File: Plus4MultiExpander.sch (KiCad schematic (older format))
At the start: 11 parts, among them CN1 EDGE_CONN, CN2 C16_NEWSTYLE_EXP_PORT_1, CN3 C16_NEWSTYLE_EXP_PORT_2, CN4 C16_NEWSTYLE_EXP_PORT_3, U1 74LS245, U2 74LS245

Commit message: Add 3D model of connector
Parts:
- CN2, CN3, CN4: MouserPN (none) -> 571-5530843-4
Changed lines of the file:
@@
 F 2 "Plus4MultiExpander:C64-Cart-Socket-Vertical" H 5425 960 50  0001 C CNN
 F 3 "DOCUMENTATION" H 5425 860 50  0001 C CNN
+F 4 "571-5530843-4" H 5425 2410 50  0001 C CNN "MouserPN"
 	1    5425 2410
 	1    0    0    -1
@@
 F 2 "Plus4MultiExpander:C64-Cart-Socket-Vertical" H 5425 4365 50  0001 C CNN
 F 3 "DOCUMENTATION" H 5425 4265 50  0001 C CNN
+F 4 "571-5530843-4" H 5425 5815 50  0001 C CNN "MouserPN"
 	1    5425 5815
 	1    0    0    -1
@@
 F 2 "Plus4MultiExpander:C64-Cart-Socket-Vertical" H 2395 4365 50  0001 C CNN
 F 3 "DOCUMENTATION" H 2395 4265 50  0001 C CNN
+F 4 "571-5530843-4" H 2395 5815 50  0001 C CNN "MouserPN"
 	1    2395 5815
 	1    0    0    -1

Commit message: Add credits and license
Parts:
- added C3: 220u, Capacitor_THT:CP_Radial_D8.0mm_P3.50mm, symbol Device:CP1
- added V0: LICENSE, Plus4MultiExpander:cc_by_nc_sa, symbol void:Void
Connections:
- wire segments 267 -> 269
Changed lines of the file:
@@
 Sheet 1 1
 Title "Plus4MultiExpander"
-Date "2023-07-26"
+Date "2023-08-03"
 Rev "1git"
 Comp "SukkoPera"
 Comment1 "Inspired by Solder/Synergy's Expansionport-Splitter"
-Comment2 ""
+Comment2 "Licensed under CC BY-NC-SA 4.0"
 Comment3 ""
 Comment4 ""
@@
 Text Notes 9710 4580 0    50   ~ 0
 C2 CREATION
+$Comp
+L power:+5V #PWR018
+U 1 1 66854472
+P 10245 2750
+F 0 "#PWR018" H 10245 2600 50  0001 C CNN
+F 1 "+5V" H 10260 2923 50  0000 C CNN
+F 2 "" H 10245 2750 50  0001 C CNN
+F 3 "" H 10245 2750 50  0001 C CNN
+	1    10245 2750
+	1    0    0    -1
+$EndComp
+Wire Wire Line
+	10245 2750 10245 2860
+Wire Wire Line
+	10245 3160 10245 3270
+$Comp
+L power:GND #PWR019
+U 1 1 6685447E
+P 10245 3270
+F 0 "#PWR019" H 10245 3020 50  0001 C CNN
+F 1 "GND" H 10250 3097 50  0000 C CNN
+F 2 "" H 10245 3270 50  0001 C CNN
+F 3 "" H 10245 3270 50  0001 C CNN
+	1    10245 3270
+	-1   0    0    -1
+$EndComp
 Wire Bus Line
 	1045 2645 1045 3345
@@
 Wire Bus Line
 	1045 5865 1045 6565
+$Comp
+L Device:CP1 C3
+U 1 1 66870BF0
+P 10245 3010
+F 0 "C3" H 10360 3056 50  0000 L CNN
+F 1 "220u" H 10360 2965 50  0000 L CNN
+F 2 "Capacitor_THT:CP_Radial_D8.0mm_P3.50mm" H 10245 3010 50  0001 C CNN
+F 3 "~" H 10245 3010 50  0001 C CNN
+	1    10245 3010
+	1    0    0    -1
+$EndComp
+$Comp
+L void:Void V0
+U 1 1 66878EB4
+P 6540 7655
+F 0 "V0" H 6618 7701 50  0000 L CNN
+F 1 "LICENSE" H 6618 7610 50  0000 L CNN
+F 2 "Plus4MultiExpander:cc_by_nc_sa" H 6540 7655 50  0001 C CNN
+F 3 "" H 6540 7655 50  0001 C CNN
+	1    6540 7655
+	1    0    0    -1
+$EndComp
 $EndSCHEMATC

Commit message: Generate /C2 with NAND gate
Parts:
- removed D1, D2: 1n4148, Diode_THT:D_DO-35_SOD27_P7.62mm_Horizontal, symbol Device:D
- removed R1: 4.7k, Resistor_THT:R_Axial_DIN0204_L3.6mm_D1.6mm_P7.62mm_Horizontal, symbol Device:R
- added C4: 100n, Capacitor_THT:C_Disc_D7.0mm_W2.5mm_P5.00mm, symbol Device:C
- added U3: 74HCT00, Package_DIP:DIP-14_W7.62mm_Socket_LongPads, symbol 74xx:74HCT00
- U1, U2: value 74LS245 -> 74HCT245
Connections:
- wire segments 269 -> 287
- no-connect marks 0 -> 2
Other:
- note added: "C2 GENERATION"
- note added: "POWER"
- note added: "SPARES"
- note removed: "C2 CREATION"
- moved on the sheet: C3

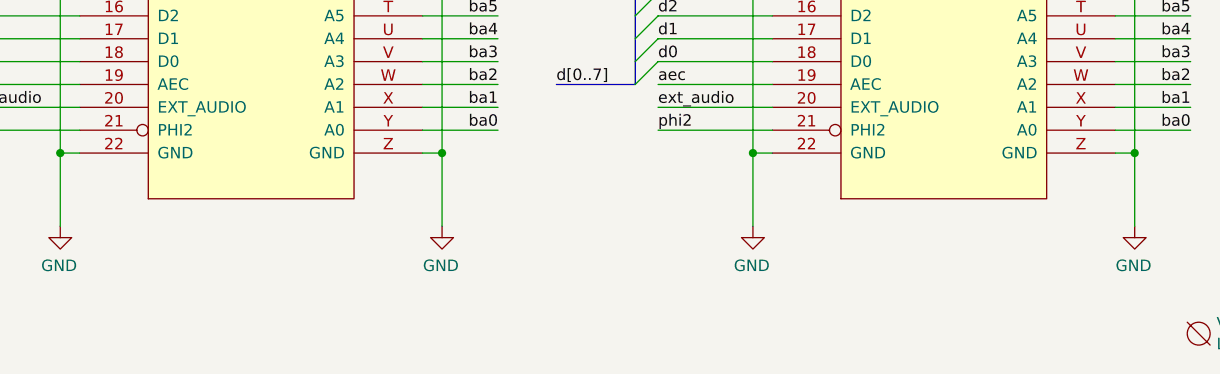
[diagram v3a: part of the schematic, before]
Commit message: Add standoff holes
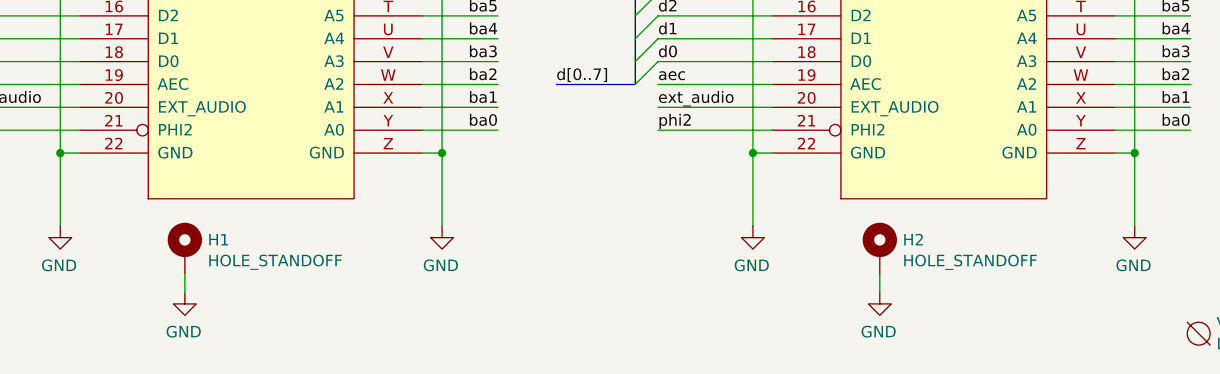
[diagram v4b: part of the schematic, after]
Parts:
- added H1, H2: HOLE_STANDOFF, MountingHole:MountingHole_2.5mm_Pad, symbol Mechanical:MountingHole_Pad
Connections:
- net GND: now also H1.1, H2.1
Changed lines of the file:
@@
 Text Notes 7620 5715 0    50   ~ 0
 SPARES
+$Comp
+L Mechanical:MountingHole_Pad H1
+U 1 1 653ED8E7
+P 2105 7295
+F 0 "H1" H 2205 7344 50  0000 L CNN
+F 1 "HOLE_STANDOFF" H 2205 7253 50  0000 L CNN
+F 2 "MountingHole:MountingHole_2.5mm_Pad" H 2105 7295 50  0001 C CNN
+F 3 "~" H 2105 7295 50  0001 C CNN
+	1    2105 7295
+	1    0    0    -1
+$EndComp
+$Comp
+L power:GND #PWR023
+U 1 1 653EEC4A
+P 2105 7475
+F 0 "#PWR023" H 2105 7225 50  0001 C CNN
+F 1 "GND" H 2110 7302 50  0000 C CNN
+F 2 "" H 2105 7475 50  0001 C CNN
+F 3 "" H 2105 7475 50  0001 C CNN
+	1    2105 7475
+	-1   0    0    -1
+$EndComp
+Wire Wire Line
+	2105 7475 2105 7395
+$Comp
+L Mechanical:MountingHole_Pad H2
+U 1 1 6542A464
+P 5145 7295
+F 0 "H2" H 5245 7344 50  0000 L CNN
+F 1 "HOLE_STANDOFF" H 5245 7253 50  0000 L CNN
+F 2 "MountingHole:MountingHole_2.5mm_Pad" H 5145 7295 50  0001 C CNN
+F 3 "~" H 5145 7295 50  0001 C CNN
+	1    5145 7295
+	1    0    0    -1
+$EndComp
+$Comp
+L power:GND #PWR024
+U 1 1 6542AB06
+P 5145 7475
+F 0 "#PWR024" H 5145 7225 50  0001 C CNN
+F 1 "GND" H 5150 7302 50  0000 C CNN
+F 2 "" H 5145 7475 50  0001 C CNN
+F 3 "" H 5145 7475 50  0001 C CNN
+	1    5145 7475
+	-1   0    0    -1
+$EndComp
+Wire Wire Line
+	5145 7475 5145 7395
 Wire Bus Line
 	1045 2645 1045 3345

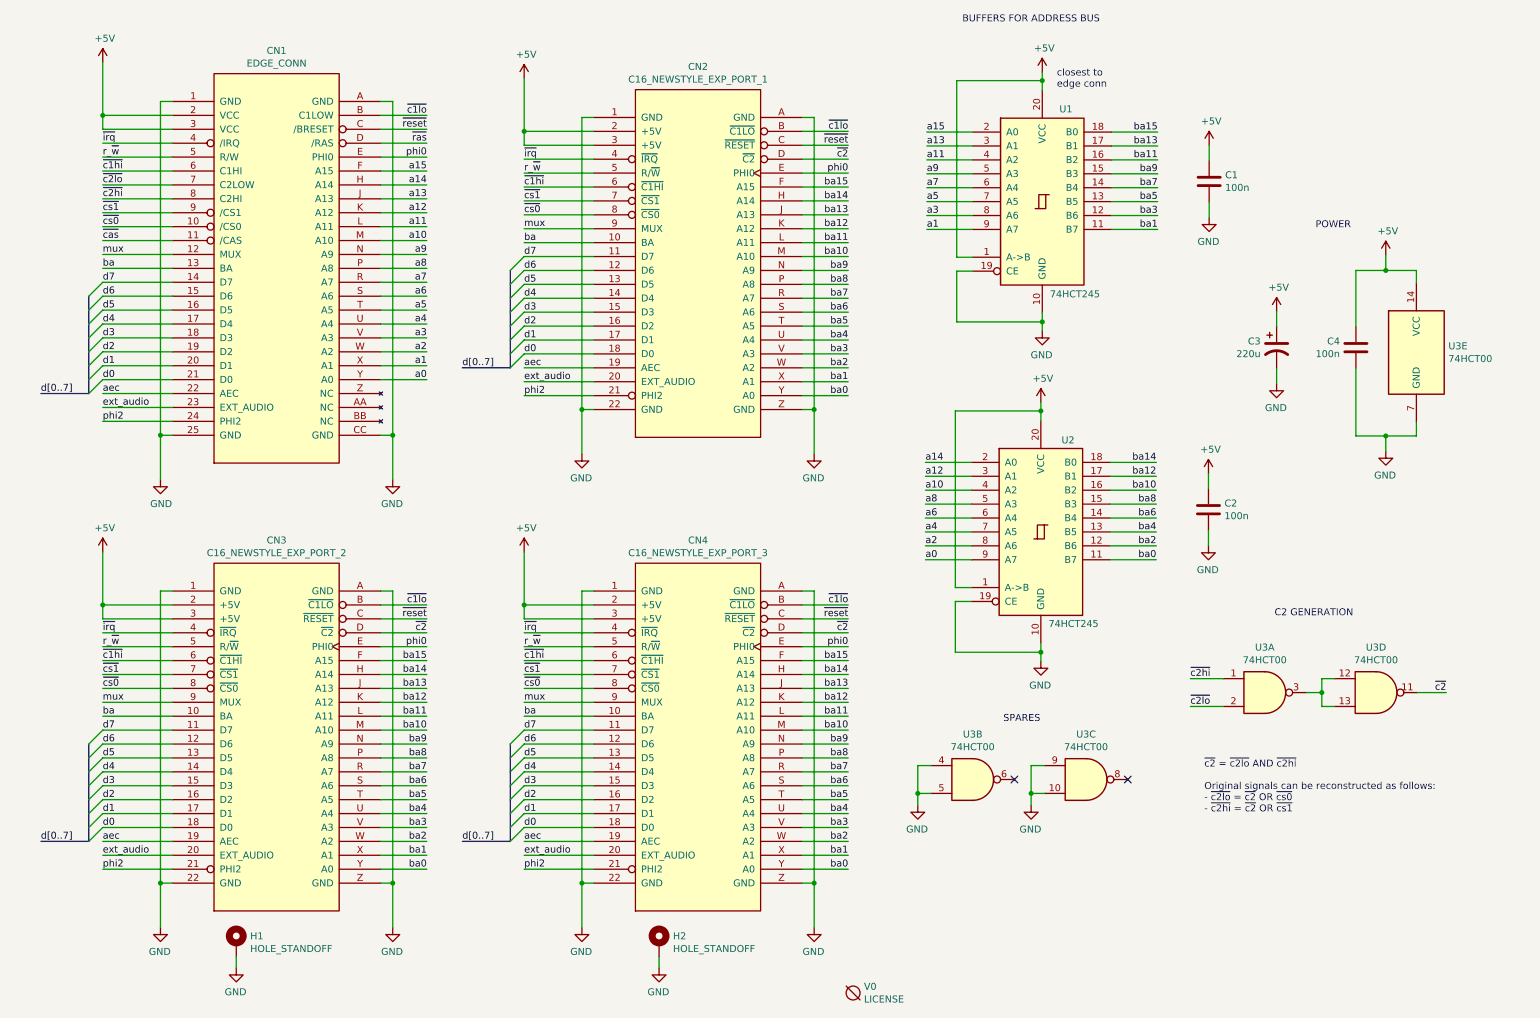
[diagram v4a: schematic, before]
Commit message: Add mixing resistors for EXT_AUDIO
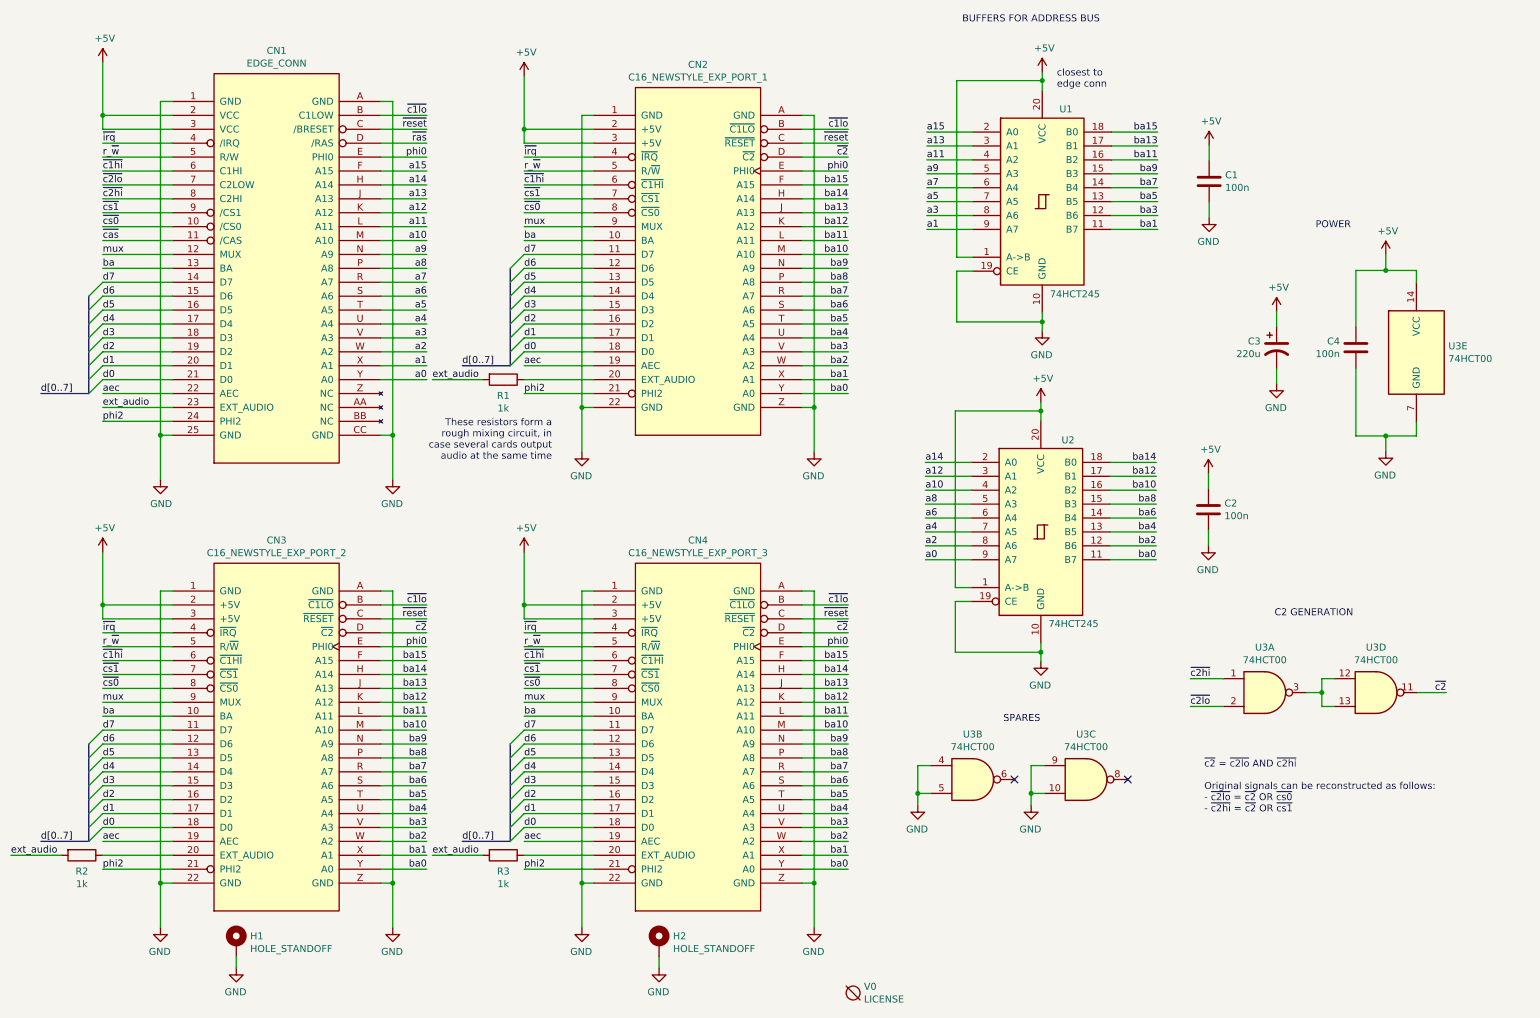
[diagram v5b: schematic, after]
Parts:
- added R1, R2, R3: 1k, Resistor_THT:R_Axial_DIN0204_L3.6mm_D1.6mm_P7.62mm_Horizontal, symbol Device:R
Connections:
- net ext_audio: now also R1.2, R2.2, R3.2; no longer CN2.20 (EXT_AUDIO), CN3.20 (EXT_AUDIO), CN4.20 (EXT_AUDIO)
- new net: CN4.20 (EXT_AUDIO), R3.1
- new net: CN3.20 (EXT_AUDIO), R2.1
- new net: CN2.20 (EXT_AUDIO), R1.1
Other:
- note added: "These resistors form a\nrough mixing circuit, in\ncase several cards output\naudio at the same time"

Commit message: Switch to AND gate and buffer some more signals
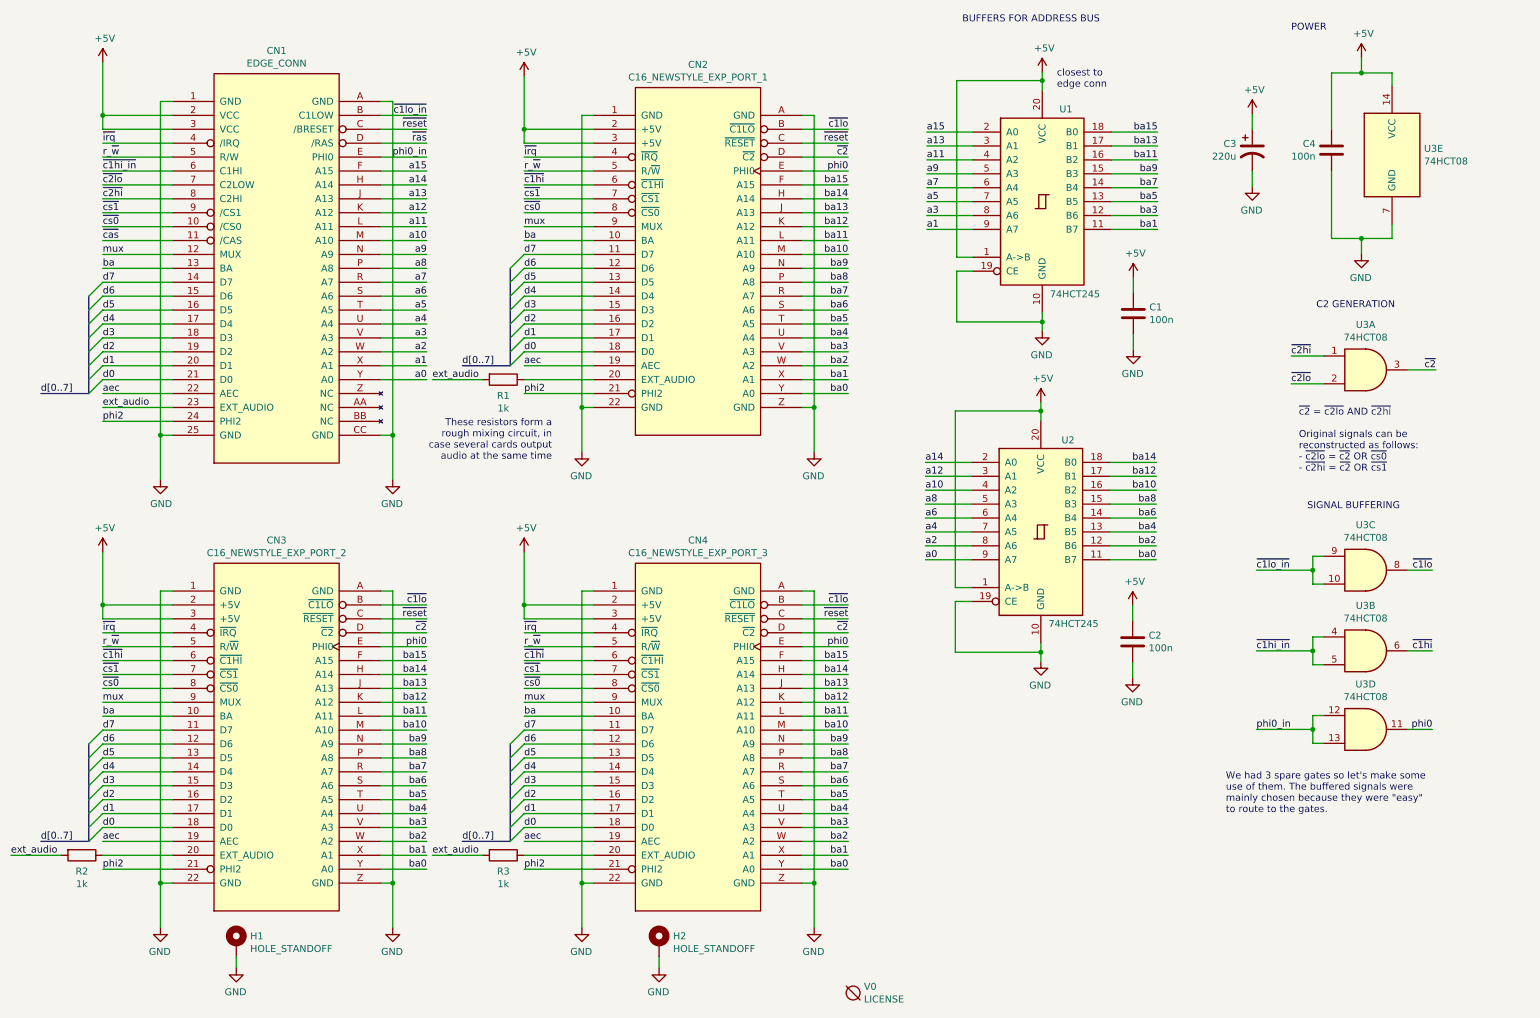
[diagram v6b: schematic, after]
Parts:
- removed U3: 74HCT00, Package_DIP:DIP-14_W7.62mm_Socket_LongPads, symbol 74xx:74HCT00
- added U3: 74HCT08, Package_DIP:DIP-14_W7.62mm_Socket_LongPads, symbol 74xx:74LS08
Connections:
- net +5V: now also U3.14 (VCC)
- net GND: now also U3.7 (GND)
- net phi0: now also U3.11; no longer CN1.E (PHI0)
- net ~c1hi: now also U3.6; no longer CN1.6 (C1HI)
- net ~c1lo: now also U3.8; no longer CN1.B (C1LOW)
- net ~c2: now also U3.3
- net ~c2hi: now also U3.1
- net ~c2lo: now also U3.2
- new net phi0_in: CN1.E (PHI0), U3.12, U3.13
- new net ~c1hi_in: CN1.6 (C1HI), U3.4, U3.5
- new net ~c1lo_in: CN1.B (C1LOW), U3.10, U3.9
- no-connect marks 2 -> 0
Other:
- note added: "SIGNAL BUFFERING"
- note added: "We had 3 spare gates so let's make some\nuse of them. The buffered signals were\nmainly chosen because they were "easy"\nto route to the gates."
- note added: "~c2~ = ~c2lo~ AND ~c2hi~\n\nOriginal signals can be\nreconstructed as follows:\n- ~c2lo~ = ~c2~ OR ~cs0~\n- ~c2hi~ = ~c2~ OR ~cs1~"
- note removed: "SPARES"
- note removed: "~c2~ = ~c2lo~ AND ~c2hi~\n\nOriginal signals can be reconstructed as follows:\n- ~c2lo~ = ~c2~ OR ~cs0~\n- ~c2hi~ = ~c2~ OR ~cs1~"
- moved on the sheet: C1, C2, C3, C4
